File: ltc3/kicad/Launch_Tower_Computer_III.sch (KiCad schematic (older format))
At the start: 0 parts

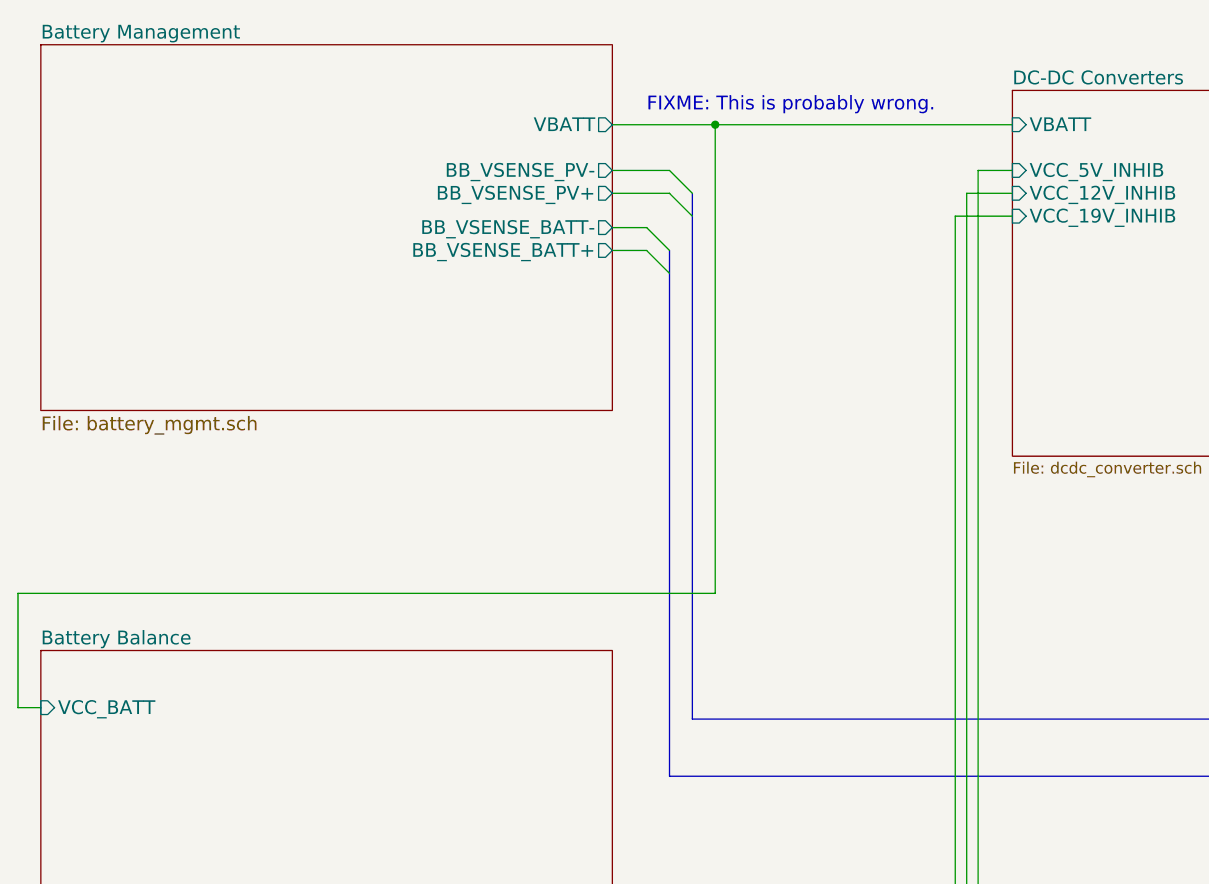
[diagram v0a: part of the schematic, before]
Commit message: LTC3: Renamed input power and battery sub-sheets.
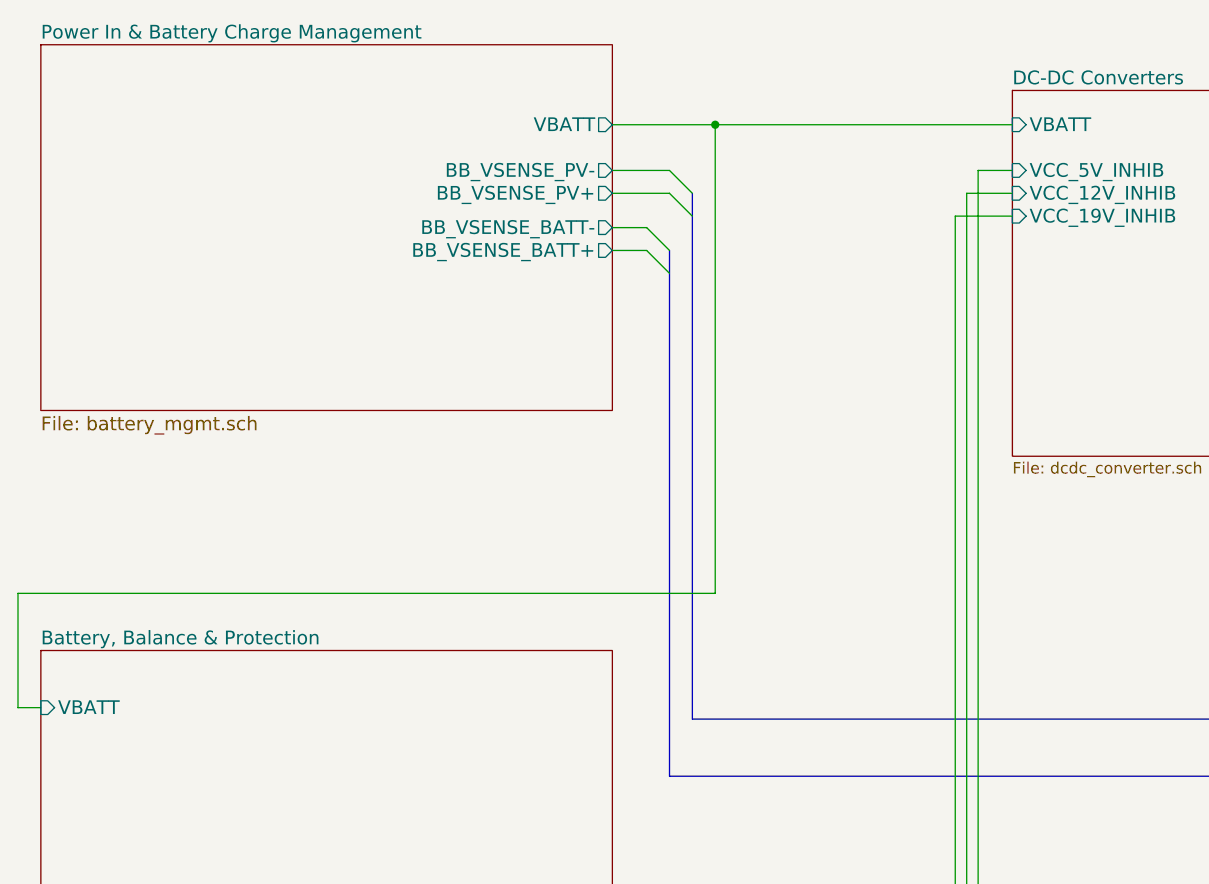
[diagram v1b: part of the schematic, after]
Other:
- note removed: "FIXME: This is probably wrong."
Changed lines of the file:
@@
 S 1000 1700 2500 1600
 U 56238165
-F0 "Battery Management" 60
+F0 "Power In & Battery Charge Management" 60
 F1 "battery_mgmt.sch" 60
 F2 "BB_VSENSE_PV-" O R 3500 2250 60
@@
 S 1000 4350 2500 1600
 U 562DD32F
-F0 "Battery Balance" 60
+F0 "Battery, Balance & Protection" 60
 F1 "battery_balance.sch" 60
 F2 "BB_TEMP_BATT+" O R 3500 5600 60
 F3 "BB_TEMP_BATT-" O R 3500 5700 60
-F4 "VCC_BATT" I L 1000 4600 60
+F4 "VBATT" I L 1000 4600 60
 $EndSheet
 $Sheet
@@
 	900  4600 1000 4600
 Connection ~ 3950 2050
-Text Notes 3650 2000 0    60   ~ 0
-FIXME: This is probably wrong.
 $EndSCHEMATC

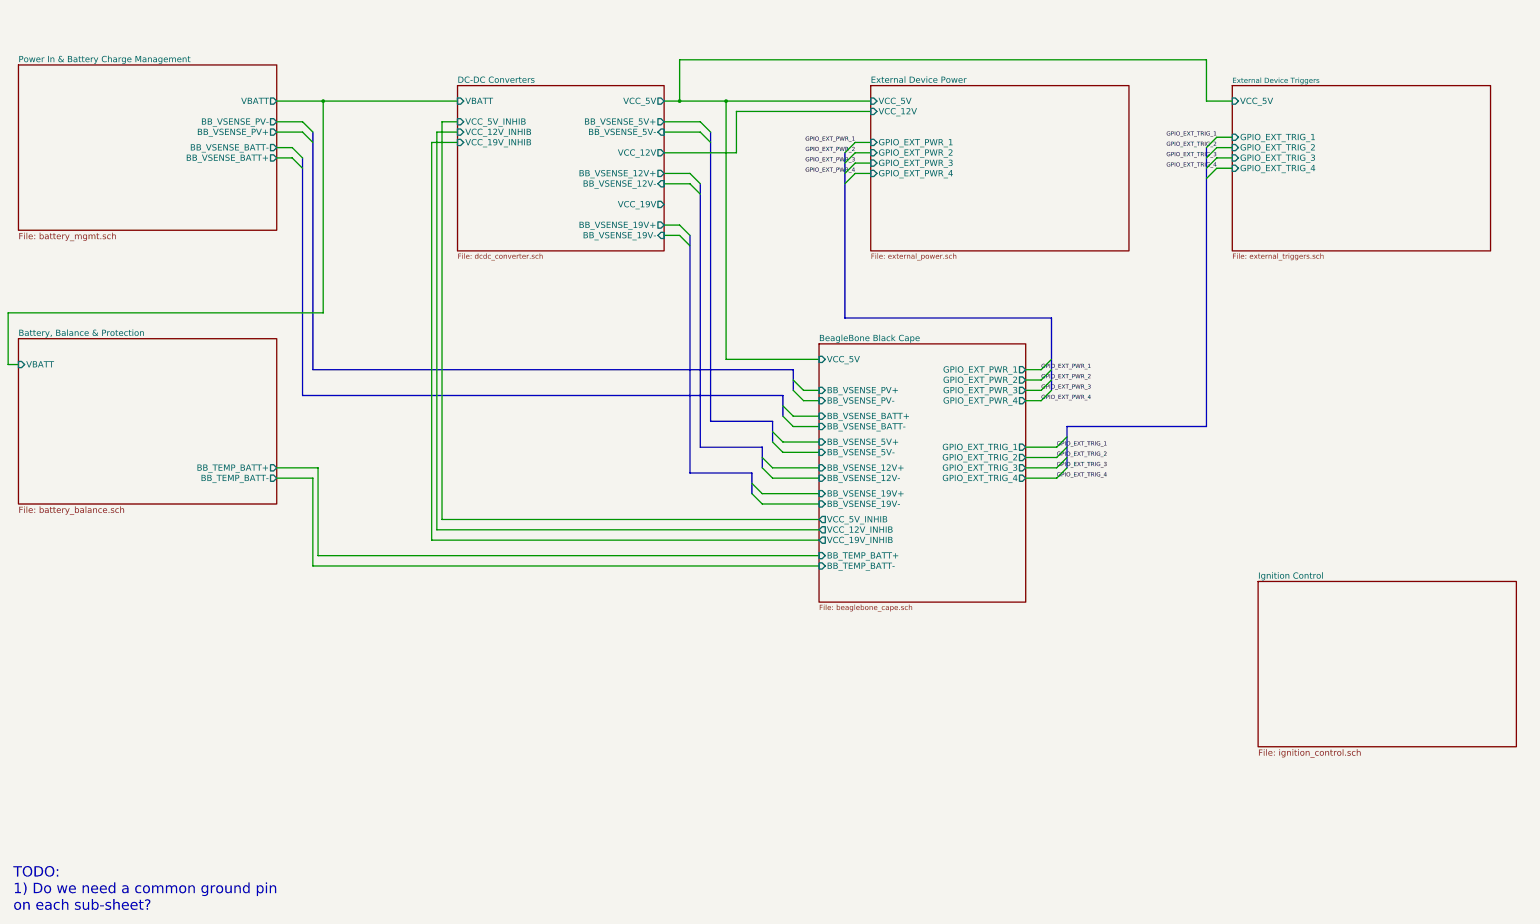
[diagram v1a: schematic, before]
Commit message: LTC3: ignition control adjustments.
1. Renamed "Ignition Control" sheet to "Rocket Interface".  Rocket I/O
   connectors will appear on this sheet.
2. Other minor adjustments to ignition control schematic (signal
   labels, etc.).
3. Added a datasheet for the ignition control circuit's schmitt
   inverter.
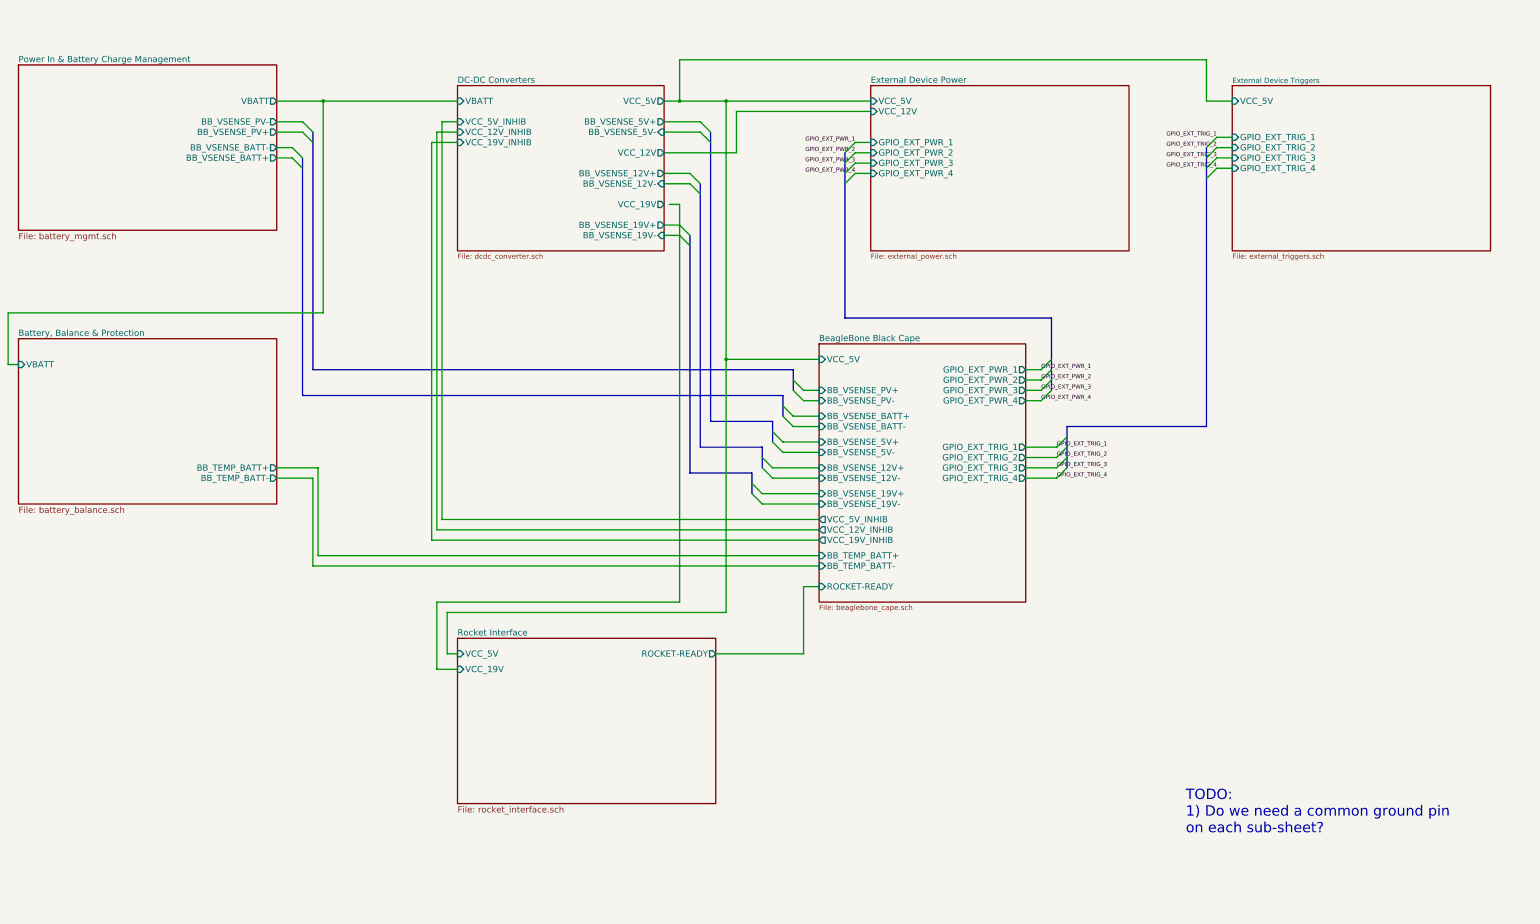
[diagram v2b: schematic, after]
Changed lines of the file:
@@
 Sheet 1 8
 Title "Launch Tower Computer 3 (LTC3)"
-Date "2015-11-07"
+Date "2015-11-16"
 Rev "A"
 Comp "Portland State Aerospace Society <http://psas.pdx.edu/>"
@@
 F24 "BB_TEMP_BATT+" I L 8750 6450 60
 F25 "BB_TEMP_BATT-" I L 8750 6550 60
-$EndSheet
-$Sheet
-S 13000 6700 2500 1600
+F26 "ROCKET-READY" I L 8750 6750 60
+$EndSheet
+$Sheet
+S 5250 7250 2500 1600
 U 5598112B
-F0 "Ignition Control" 60
-F1 "ignition_control.sch" 60
+F0 "Rocket Interface" 60
+F1 "rocket_interface.sch" 60
+F2 "VCC_5V" I L 5250 7400 60
+F3 "VCC_19V" I L 5250 7550 60
+F4 "ROCKET-READY" O R 7750 7400 60
 $EndSheet
 $Sheet
@@
 F6 "GPIO_EXT_TRIG_4" I L 12750 2700 60
 $EndSheet
-Text Notes 950  9900 0    100  ~ 0
+Text Notes 12300 9150 0    100  ~ 0
 TODO:\n1) Do we need a common ground pin\non each sub-sheet?
 Entry Wire Line
@@
 	7700 2350 7700 5150
 Wire Wire Line
-	7850 4550 7850 2050
+	7850 2050 7850 7000
 Connection ~ 7850 2050
 Wire Wire Line
@@
 	900  4600 1000 4600
 Connection ~ 3950 2050
+Wire Wire Line
+	7850 7000 5150 7000
+Wire Wire Line
+	5150 7000 5150 7400
+Wire Wire Line
+	5150 7400 5250 7400
+Connection ~ 7850 4550
+Wire Wire Line
+	7300 3050 7400 3050
+Wire Wire Line
+	7400 3050 7400 6900
+Wire Wire Line
+	7400 6900 5050 6900
+Wire Wire Line
+	5050 6900 5050 7550
+Wire Wire Line
+	5050 7550 5250 7550
+Wire Wire Line
+	7750 7400 8600 7400
+Wire Wire Line
+	8600 7400 8600 6750
+Wire Wire Line
+	8600 6750 8750 6750
 $EndSCHEMATC

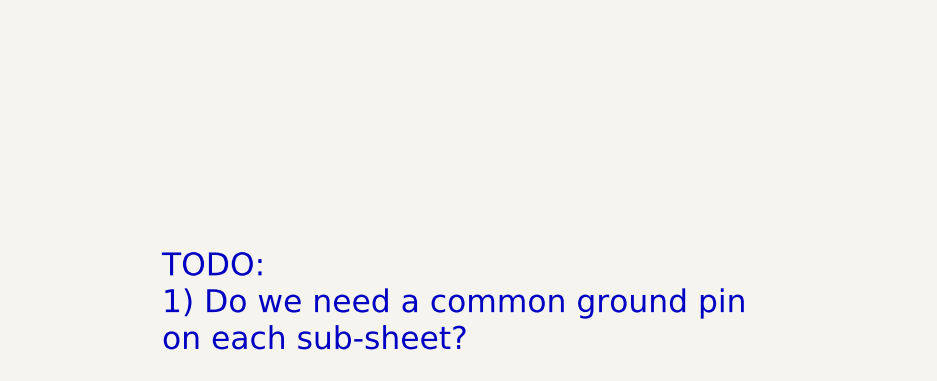
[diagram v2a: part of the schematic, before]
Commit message: LTC3: Tidied up rocket interface schematic.
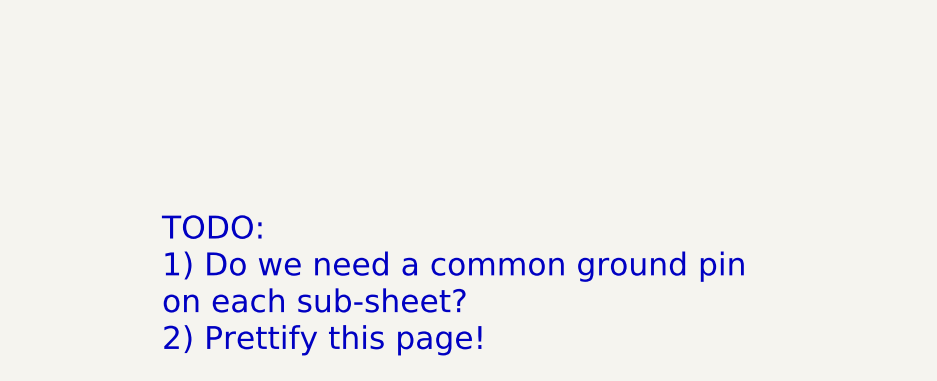
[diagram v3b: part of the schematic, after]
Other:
- note added: "TODO:\n1) Do we need a common ground pin\non each sub-sheet?\n2) Prettify this page!"
- note removed: "TODO:\n1) Do we need a common ground pin\non each sub-sheet?"
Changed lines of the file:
@@
 $EndSheet
 Text Notes 12300 9150 0    100  ~ 0
-TODO:\n1) Do we need a common ground pin\non each sub-sheet?
+TODO:\n1) Do we need a common ground pin\non each sub-sheet?\n2) Prettify this page!
 Entry Wire Line
 	7600 2250 7700 2350

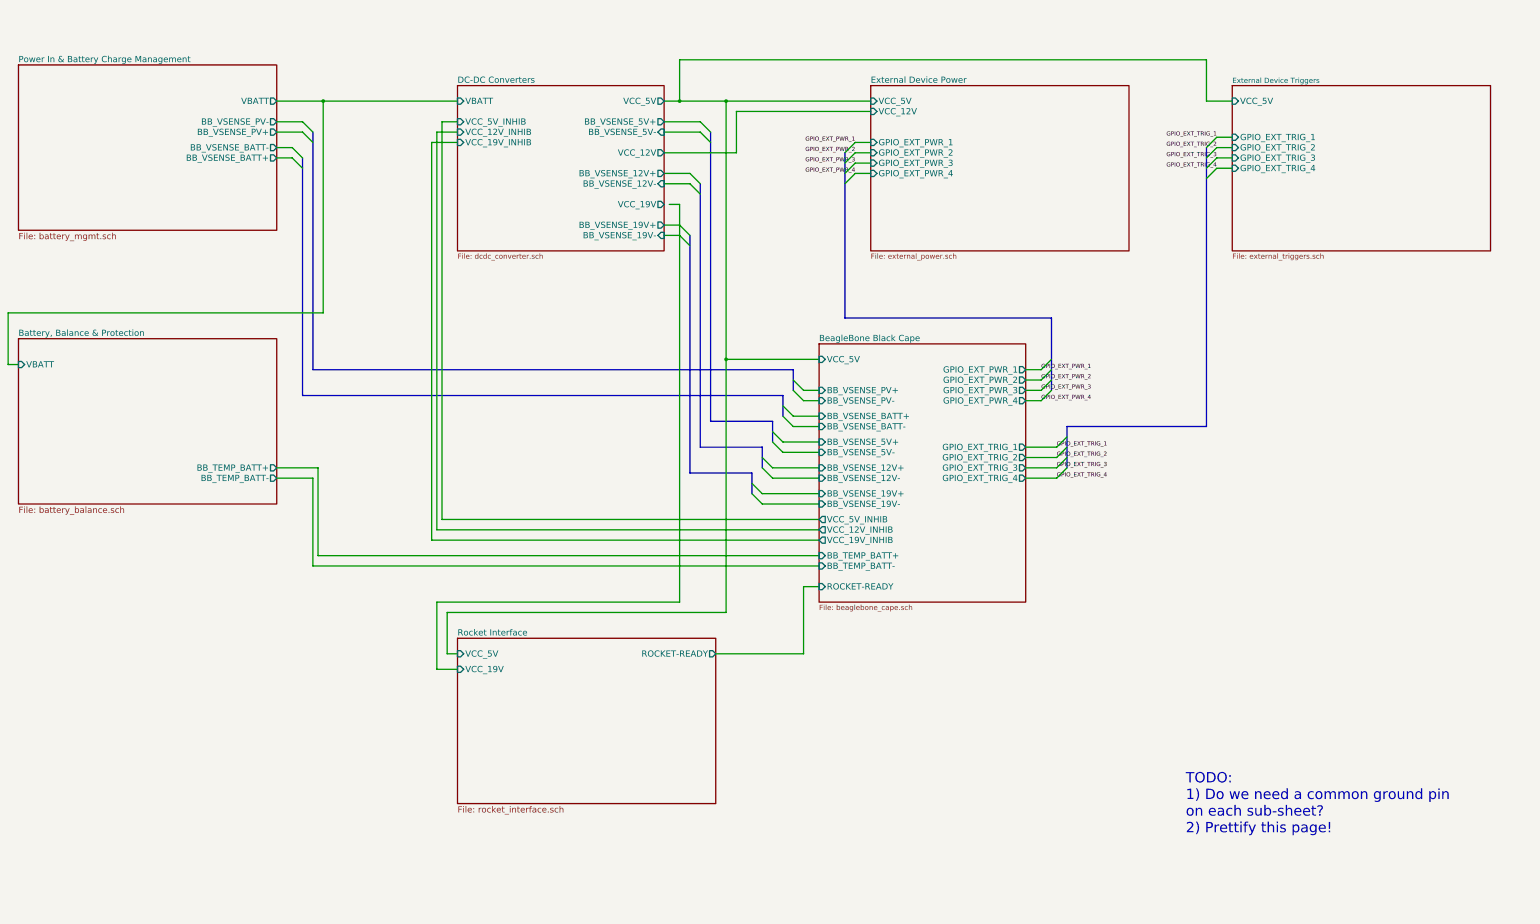
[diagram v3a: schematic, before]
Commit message: LTC3: Progress on battery management schematic.
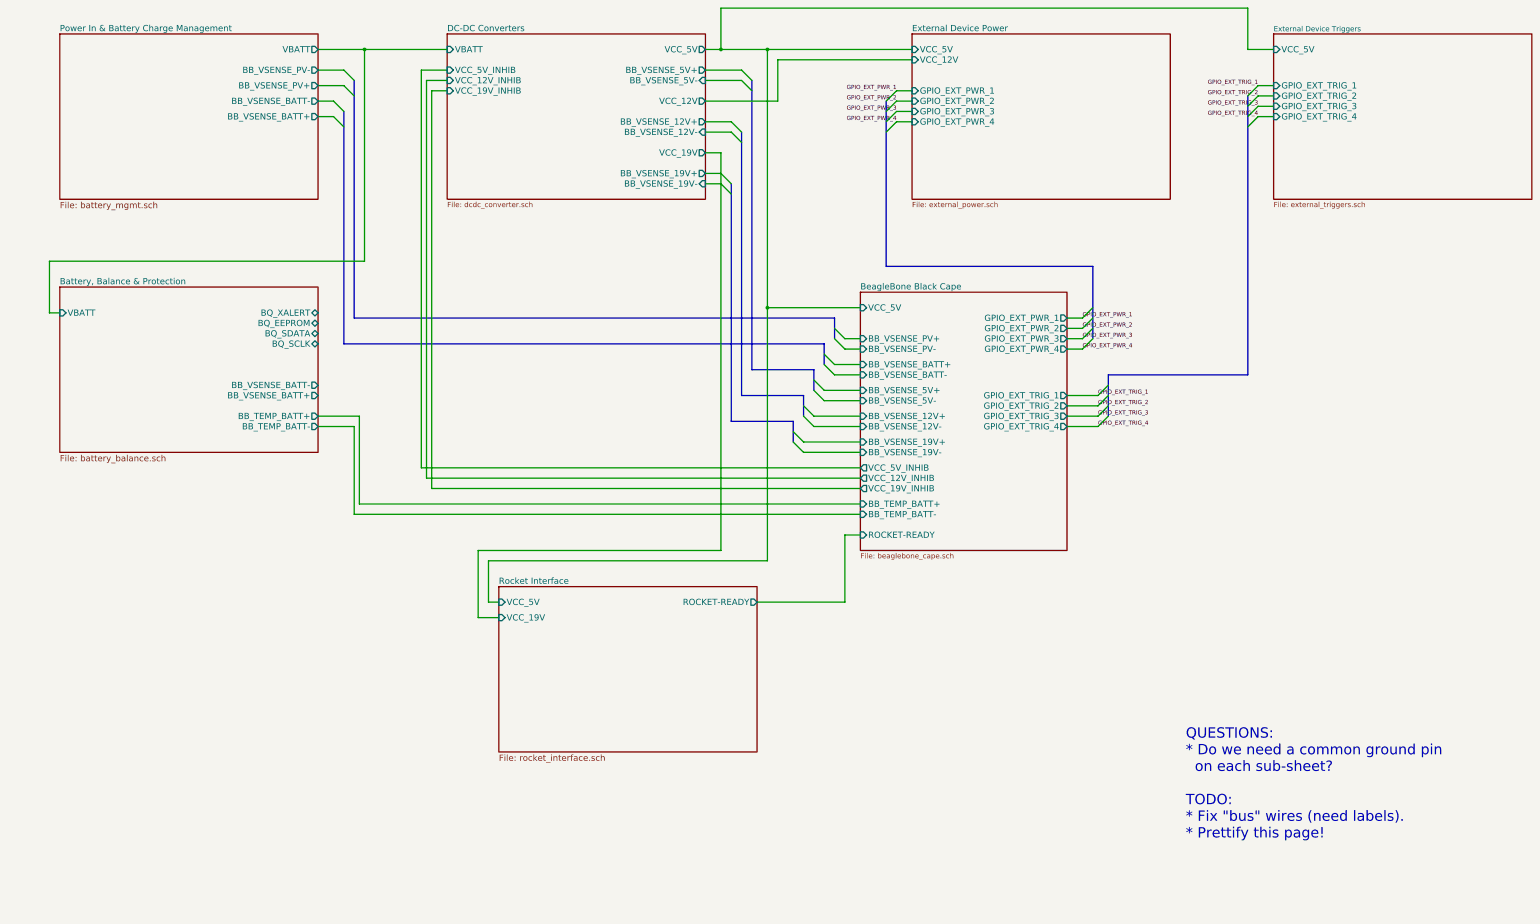
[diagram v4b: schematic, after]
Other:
- note added: "QUESTIONS:\n* Do we need a common ground pin\n on each sub-sheet?\n\nTODO:\n* Fix "bus" wires (need labels).\n* Prettify this page!"
- note removed: "TODO:\n1) Do we need a common ground pin\non each sub-sheet?\n2) Prettify this page!"
